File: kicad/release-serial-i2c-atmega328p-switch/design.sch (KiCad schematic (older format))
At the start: 34 parts, among them J17 Sense0, J3 RS232, J4 OUT0a, Q1 MMBT3904, Q2 FQP47P06, SW1 12V, U1 MCP1792T-33, U2 MCP1792T-5, U3 ATmega328P-AU, Y1 AB308-8.000MHZ

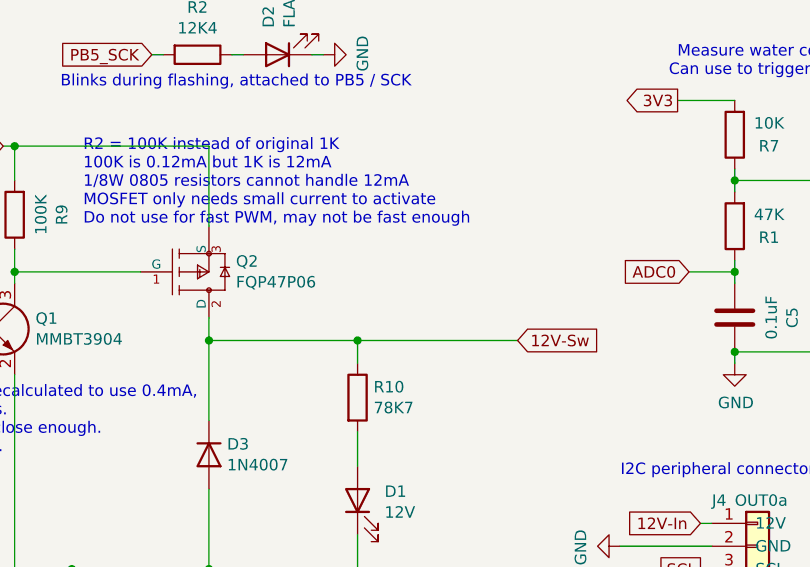
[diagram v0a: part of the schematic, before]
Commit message: Add SUP60061EL-GE3 to schematic, supports 30 amps DC instead of 10 amps from FQP47P06
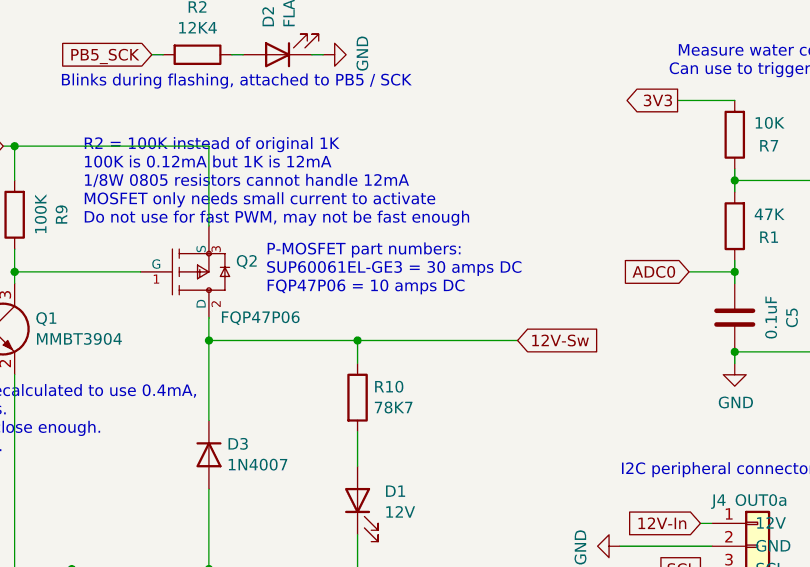
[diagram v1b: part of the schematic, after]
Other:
- note added: "P-MOSFET part numbers:\nSUP60061EL-GE3 = 30 amps DC\nFQP47P06 = 10 amps DC"
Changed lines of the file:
@@
 P 6650 1800
 F 0 "Q2" H 7168 1846 50  0000 L CNN
-F 1 "FQP47P06" H 7168 1755 50  0000 L CNN
+F 1 "FQP47P06" H 7100 1600 50  0000 L CNN
 F 2 "custom:WP_MOSFET_TO-220-3_Vertical" H 6650 2300 50  0001 L CNN
 F 3 "https://www.mouser.com/datasheet/2/308/1/FQP47P06_D-2313837.pdf" H 6650 2400 50  0001 L CNN
@@
 	9850 2150 9350 2150
 Connection ~ 9350 2150
+Text Notes 7300 1900 0    50   ~ 0
+P-MOSFET part numbers:\nSUP60061EL-GE3 = 30 amps DC\nFQP47P06 = 10 amps DC
 $EndSCHEMATC
